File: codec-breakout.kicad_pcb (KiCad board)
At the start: 2 copper layers, 59.7 x 26.7 mm, 44 parts, among them IC1 VS1053B, J1 SJ1-3523N, J2 Conn_01x07, J3 Conn_01x05, J4 Conn_01x03, J5 Conn_01x02, U1 TLV7101828DSER, Y1 ABM8G-12.288MHZ-4Y-T3

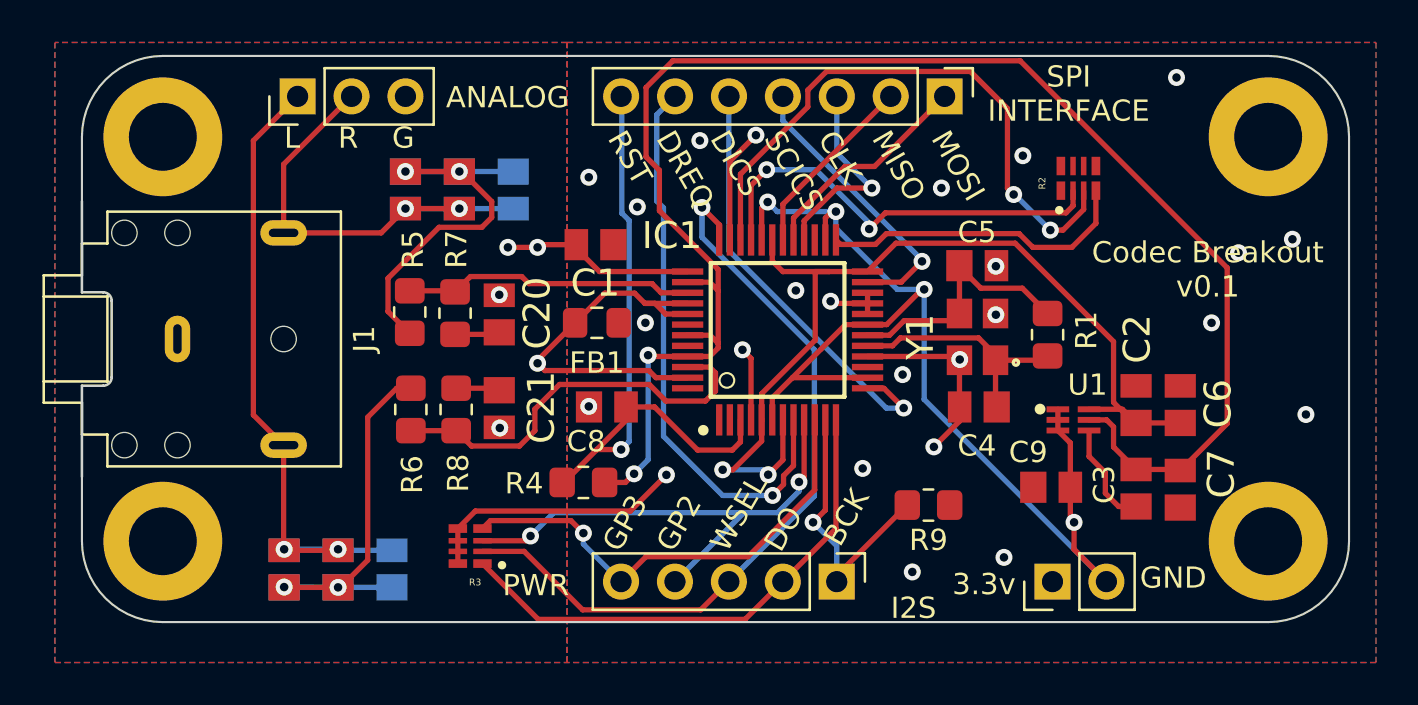
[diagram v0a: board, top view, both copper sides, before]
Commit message: Fix incorrect silkscreen
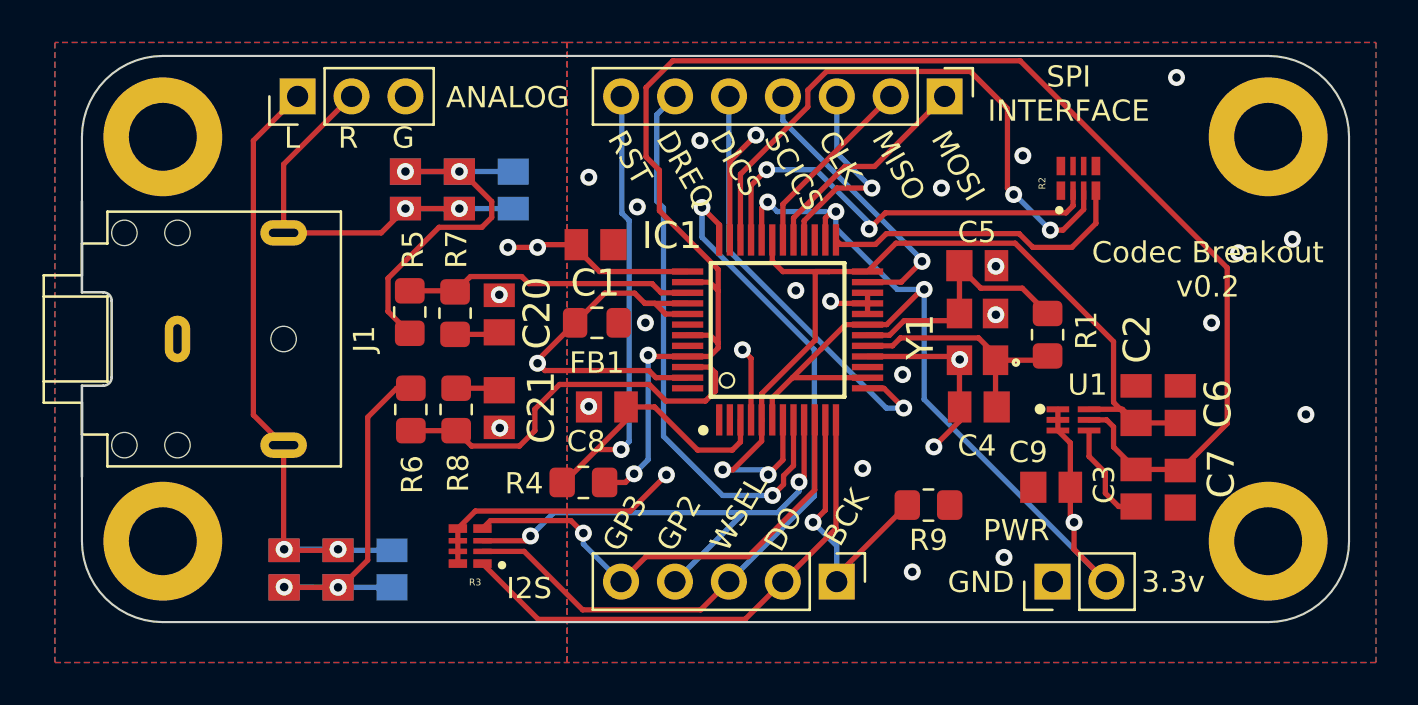
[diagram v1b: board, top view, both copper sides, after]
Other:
- board text added: "Codec Breakout v0.2"
- board text removed: "Codec Breakout v0.1"
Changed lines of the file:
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@@
     (effects (font (size 1 1) (thickness 0.15)) (justify left bottom mirror))
   )
-  (gr_text "GND" (at 209.8548 68.9864) (layer "F.SilkS")
+  (gr_text "GND" (at 200.8 69.19) (layer "F.SilkS")
     (effects (font (size 1 1) (thickness 0.15)) (justify left bottom))
   )
-  (gr_text "Codec Breakout\nv0.1" (at 213.0552 55.2704) (layer "F.SilkS")
+  (gr_text "Codec Breakout\nv0.2" (at 213.0552 55.2704) (layer "F.SilkS")
     (effects (font (size 1 1) (thickness 0.15)) (justify bottom))
   )
@@
     (effects (font (size 1 1) (thickness 0.15)) (justify left bottom))
   )
-  (gr_text "I2S" (at 198.12 70.4088) (layer "F.SilkS")
+  (gr_text "I2S" (at 180.01 69.48) (layer "F.SilkS")
     (effects (font (size 1 1) (thickness 0.15)) (justify left bottom))
   )
@@
     (effects (font (size 1 1) (thickness 0.15)) (justify left bottom))
   )
-  (gr_text "3.3v" (at 201.0156 69.2912) (layer "F.SilkS")
+  (gr_text "3.3v" (at 209.93 69.18) (layer "F.SilkS")
     (effects (font (size 1 1) (thickness 0.15)) (justify left bottom))
   )
@@
     (effects (font (size 1 1) (thickness 0.15)) (justify left bottom))
   )
-  (gr_text "PWR" (at 179.832 69.342) (layer "F.SilkS")
+  (gr_text "PWR" (at 202.47 66.75) (layer "F.SilkS")
     (effects (font (size 1 1) (thickness 0.15)) (justify left bottom))
   )
